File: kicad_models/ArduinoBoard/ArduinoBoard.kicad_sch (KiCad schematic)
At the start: 22 parts, among them J1 5V Output, J10 Conn_01x06_Pin, J2 Buttons, J3 PWM Output, J4 12V Input, J5 Conn_01x04_Pin, J6 Conn_01x04_Pin, J7 Conn_01x06_Pin, J8 Conn_01x06_Pin, J9 Conn_01x04_Pin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

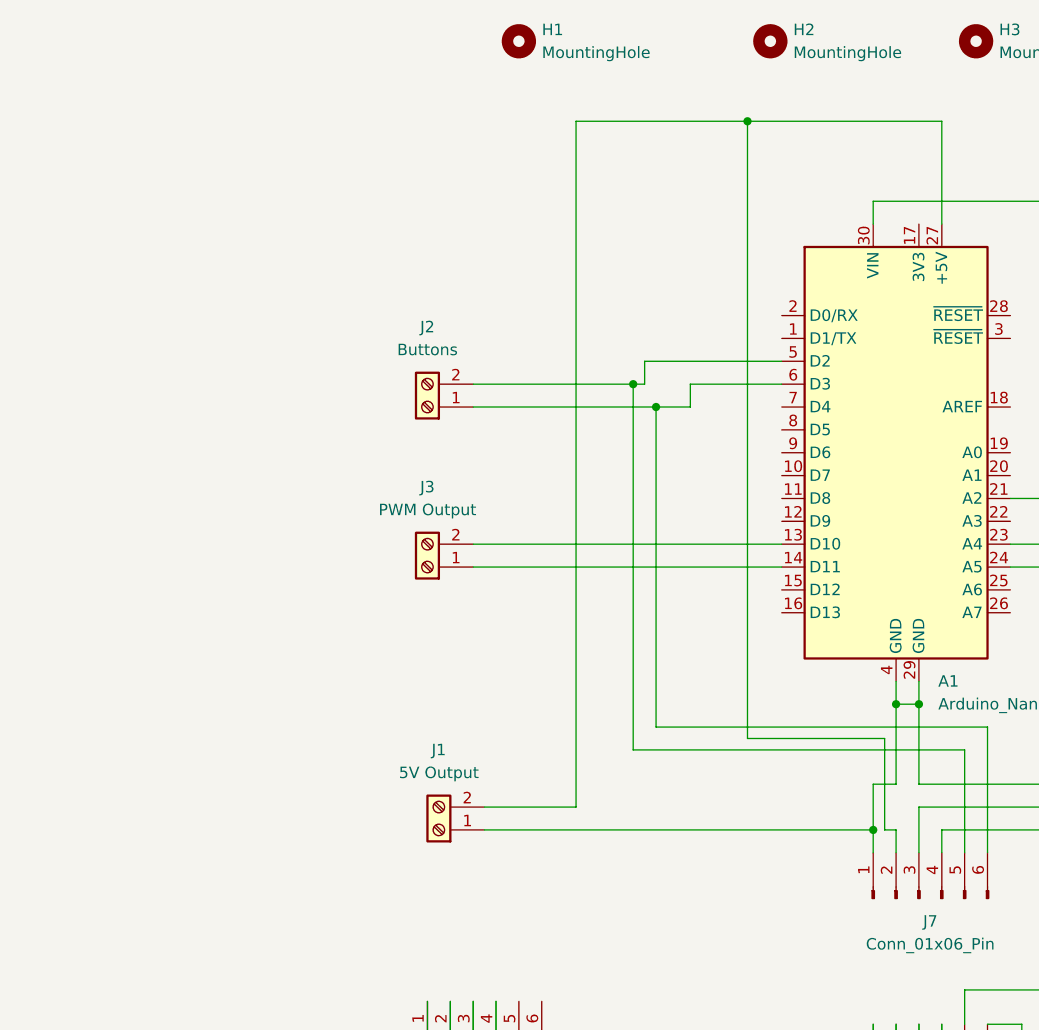
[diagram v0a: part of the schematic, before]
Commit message: Added a 2x4 (8-pin) connector to the main board which allows it to connect to the motor controller with a ribbon cable.
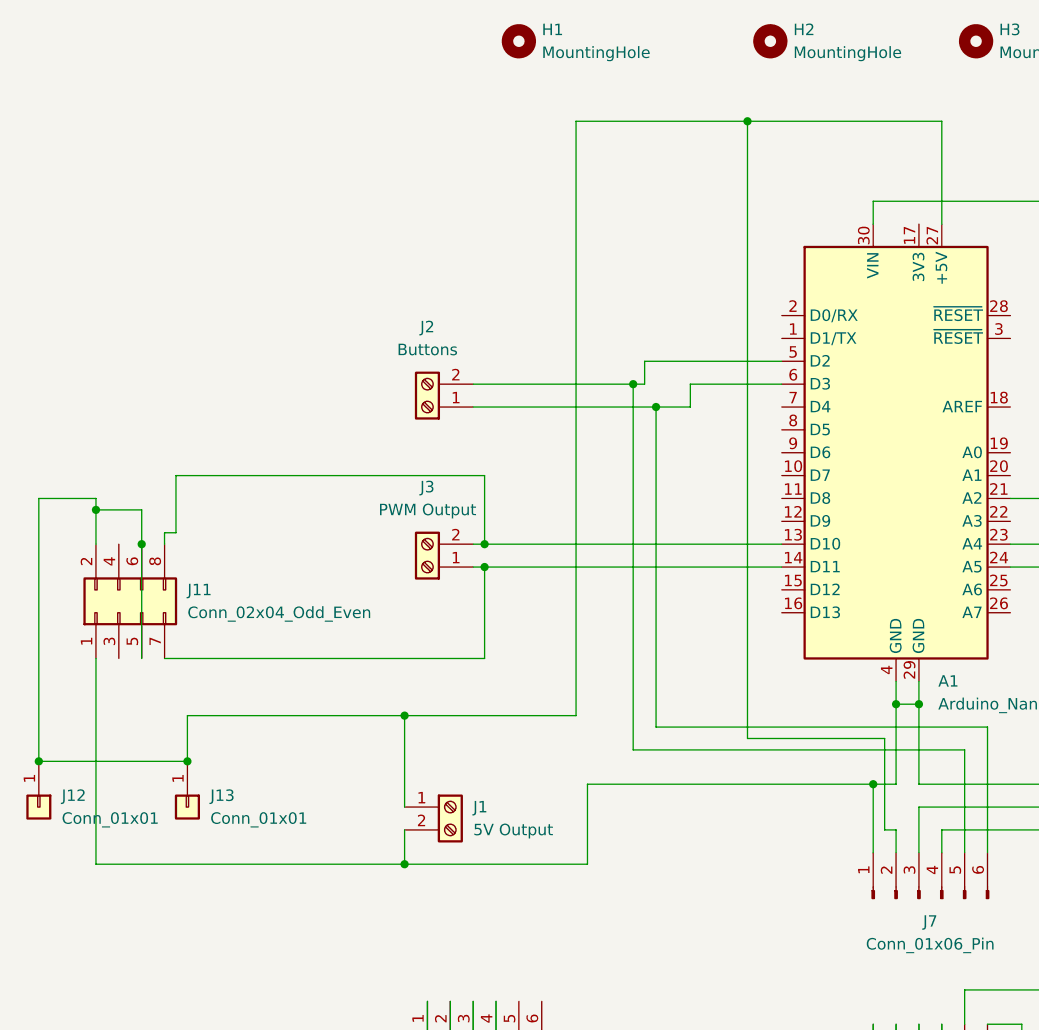
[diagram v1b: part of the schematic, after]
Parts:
- added J11: Conn_02x04_Odd_Even, Connector_PinHeader_2.54mm:PinHeader_2x04_P2.54mm_Vertical, symbol Connector_Generic:Conn_02x04_Odd_Even
- added J12, J13: Conn_01x01, Connector_PinHeader_2.54mm:PinHeader_1x01_P2.54mm_Vertical, symbol Connector_Generic:Conn_01x01
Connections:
- net GND: now also J1.2 (Pin_2), J11.1 (Pin_1); no longer J1.1 (Pin_1)
- net at A1.13 (D10), J3.2 (Pin_2): now also J11.8 (Pin_8)
- net at A1.14 (D11), J3.1 (Pin_1): now also J11.7 (Pin_7)
- net at A1.27 (+5V), J7.2 (Pin_2): now also J1.1 (Pin_1), J11.2 (Pin_2), J11.5 (Pin_5), J11.6 (Pin_6), J12.1 (Pin_1), J13.1 (Pin_1); no longer J1.2 (Pin_2)
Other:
- moved on the sheet: J1

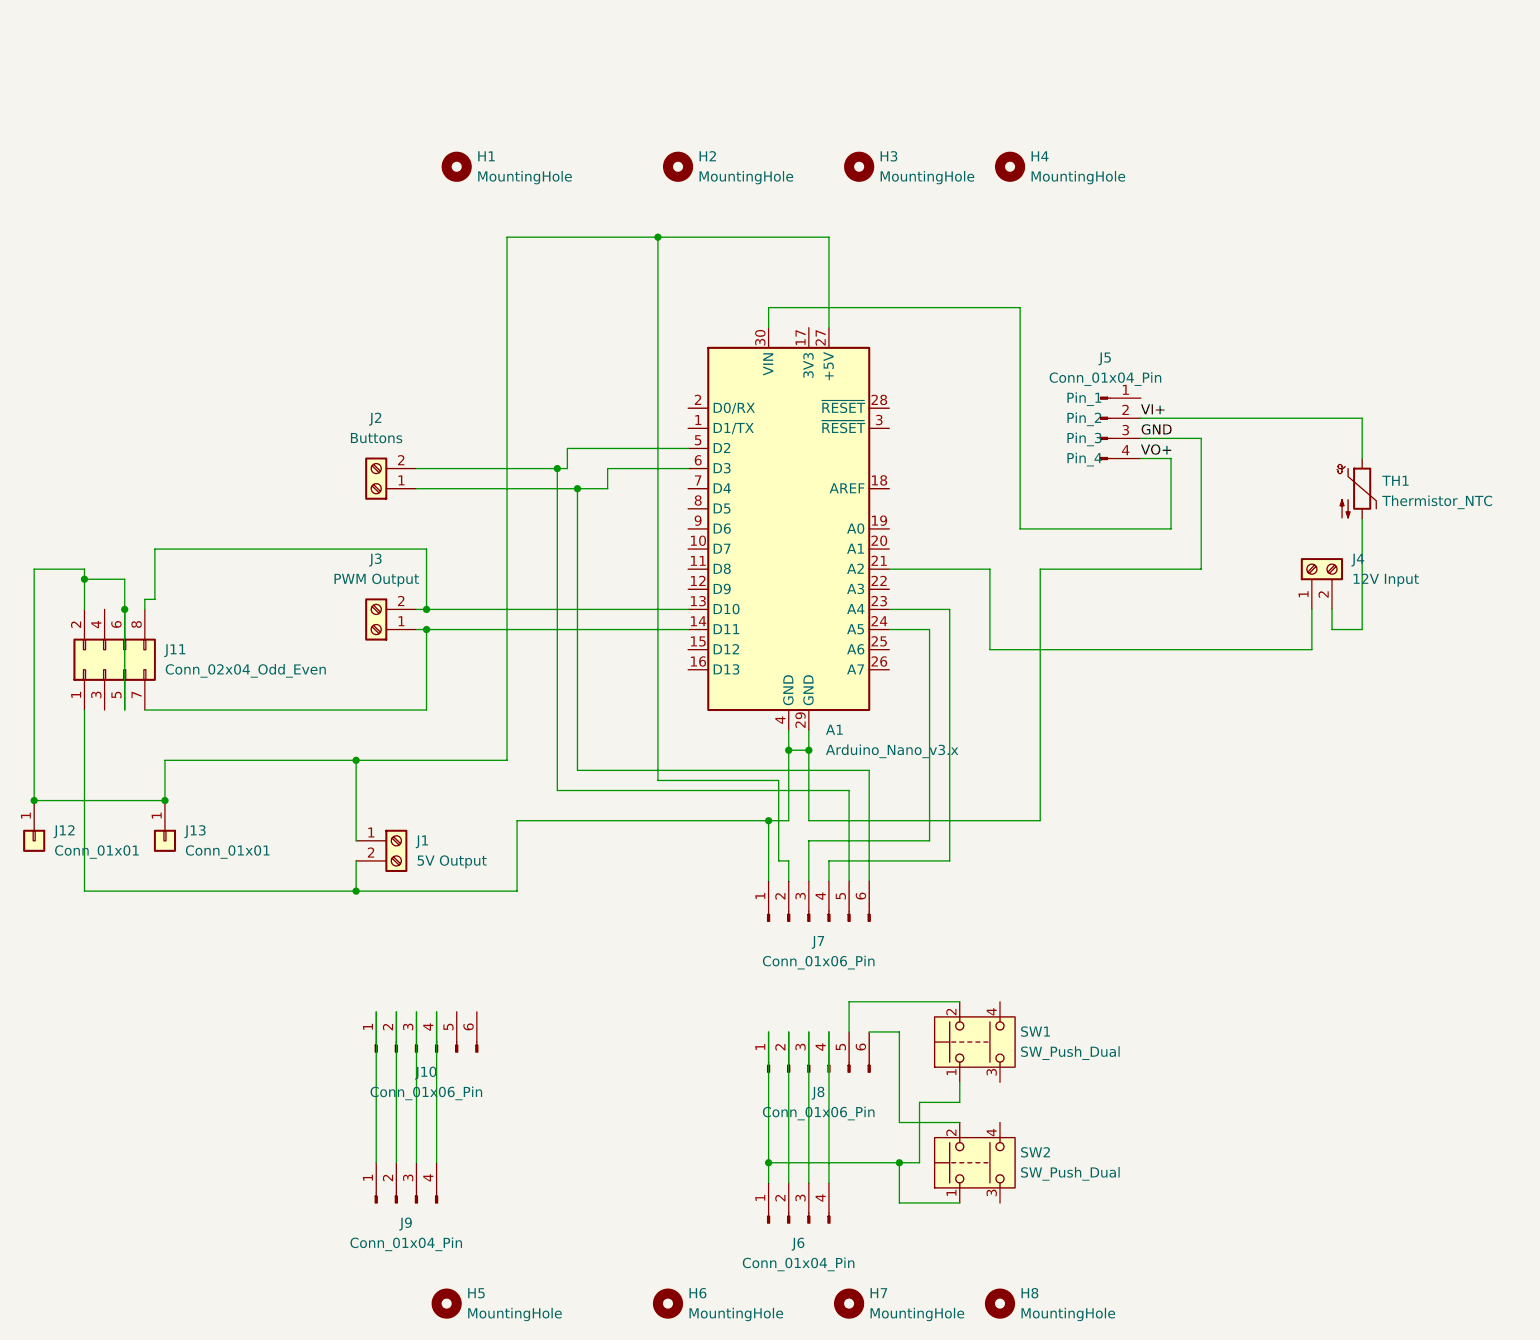
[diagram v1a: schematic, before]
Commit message: Redesigned the PCB - moved the screw terminals for the switch to the other side of the board and changed to analog GPIO (A2 & A3) rather than Digital. Moved the two screw holes that were toward the front of the gauge back about 10mm to give it some space for brass inserts. Updated the Arduino code to use the new GPIO for the switch actuation. Also updated the Solid Edge/STL files to match the new screw holes in the PCB.
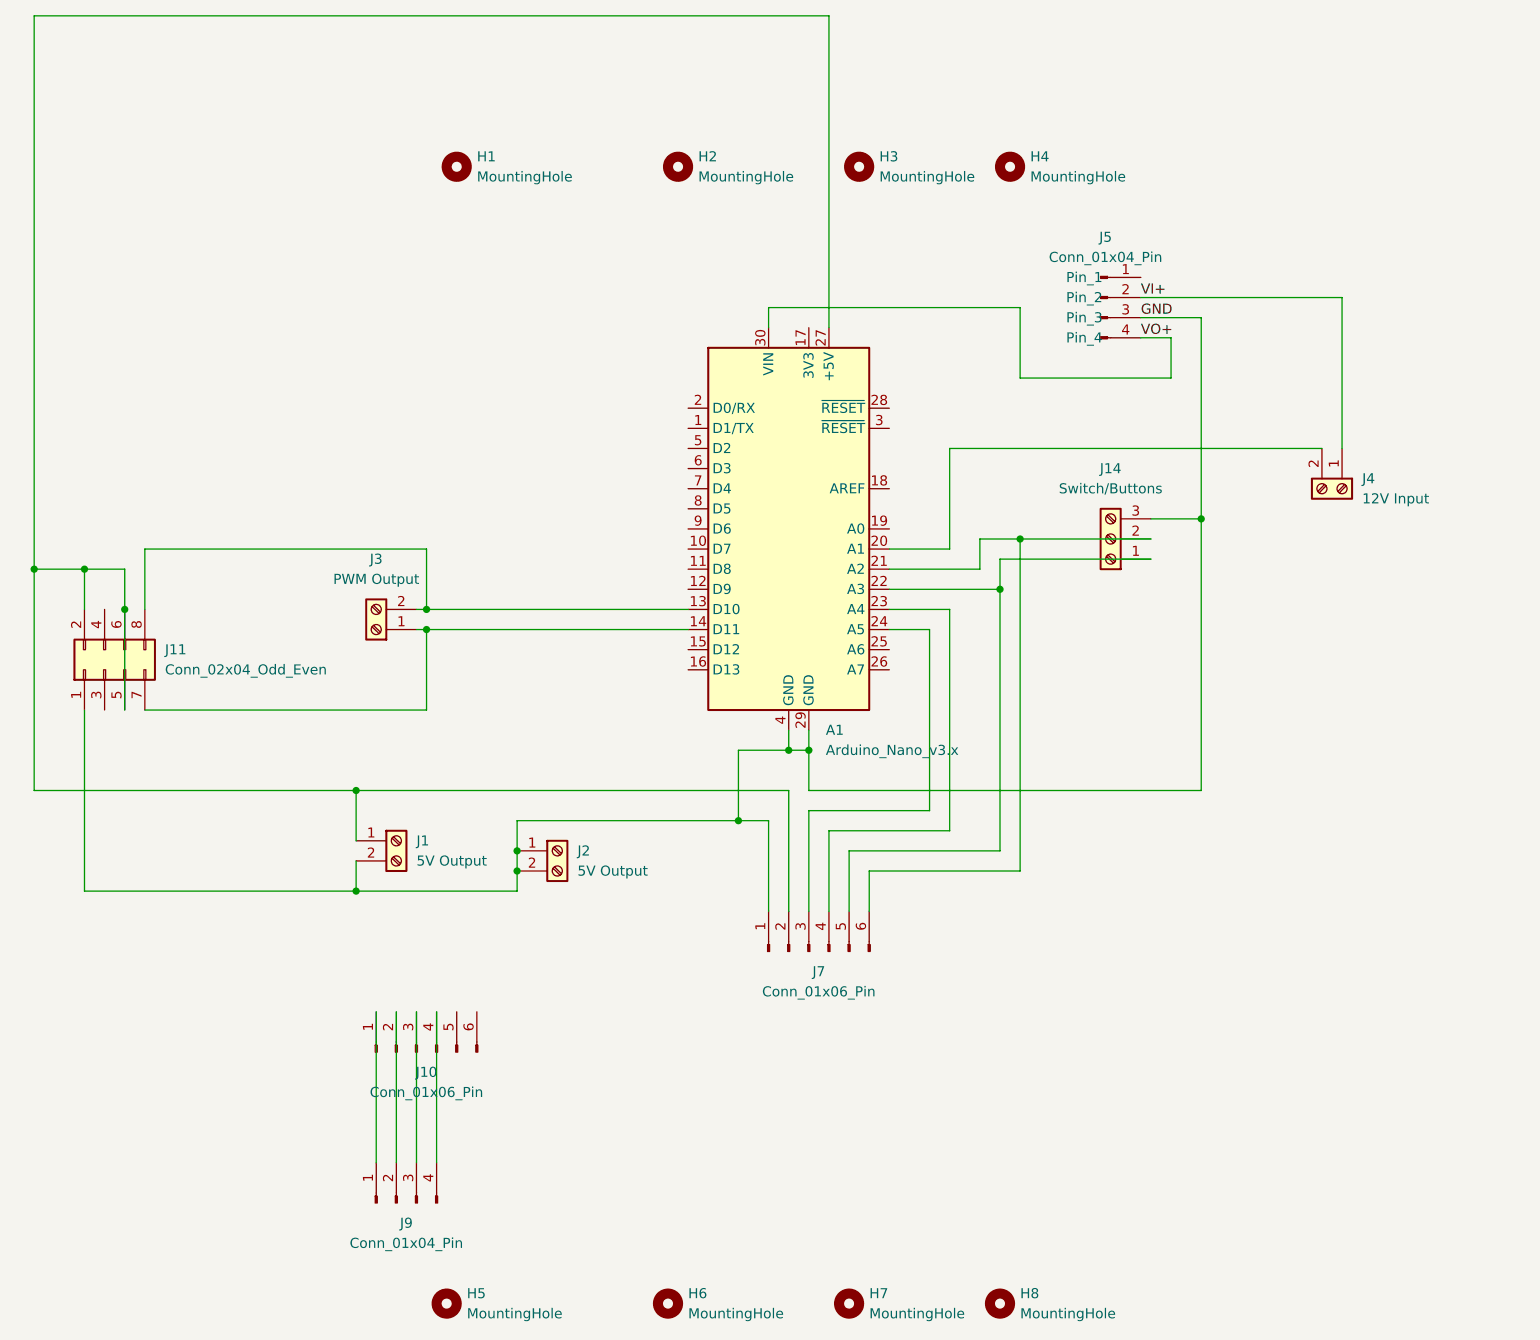
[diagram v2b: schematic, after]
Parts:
- removed J12, J13: Conn_01x01, Connector_PinHeader_2.54mm:PinHeader_1x01_P2.54mm_Vertical, symbol Connector_Generic:Conn_01x01
- removed J6: Conn_01x04_Pin, Connector_PinHeader_2.54mm:PinHeader_1x04_P2.54mm_Vertical, symbol Connector:Conn_01x04_Pin
- removed J8: Conn_01x06_Pin, Connector_PinHeader_2.54mm:PinHeader_1x06_P2.54mm_Vertical, symbol Connector:Conn_01x06_Pin
- removed SW1, SW2: SW_Push_Dual, Button_Switch_THT:SW_PUSH-12mm, symbol Switch:SW_Push_Dual
- removed TH1: Thermistor_NTC, Resistor_THT:R_Axial_DIN0204_L3.6mm_D1.6mm_P5.08mm_Vertical, symbol Device:Thermistor_NTC
- added J14: Switch/Buttons, TerminalBlock:TerminalBlock_bornier-3_P5.08mm, symbol Connector:Screw_Terminal_01x03
- J2: value Buttons -> 5V Output
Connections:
- net GND: now also J2.1 (Pin_1), J2.2 (Pin_2), J14.3 (Pin_3)
- net VI+: now also J4.1 (Pin_1)
- net at J4.2 (Pin_2): now also A1.20 (A1)
- net at A1.21 (A2): now also J7.6 (Pin_6), J14.2 (Pin_2); no longer J4.1 (Pin_1)
- net at A1.22 (A3): now also J7.5 (Pin_5), J14.1 (Pin_1)
- now unconnected: A1.5 (D2), A1.6 (D3)
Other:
- moved on the sheet: J4, J5, J7

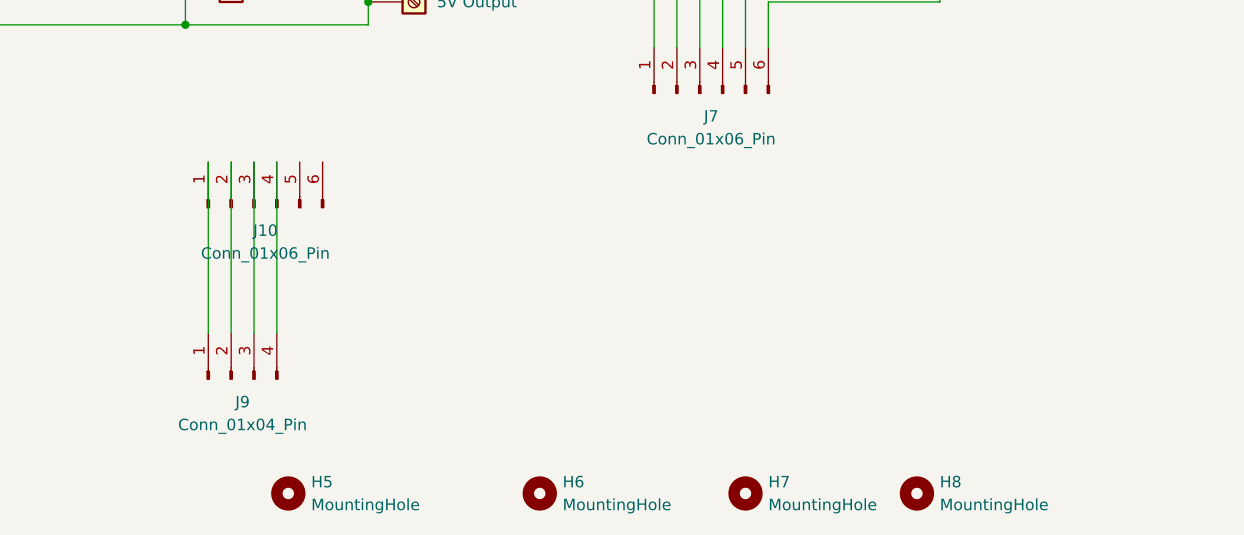
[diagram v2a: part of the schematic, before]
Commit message: Fixed a gerber file issue reported by Jon Parnaby. He noted that a lot of the through holes in the PCBs he ordered from JLCPCB were too small (for Arduino and other components). I grew the holes from .5mm to 1.0mm. I also split the PCB into two separate projects so that it would be easier to send them off to be manufactured.
Also updated the printable PDFs for PCB transfer paper (e.g. reversed, underside, copper-only).
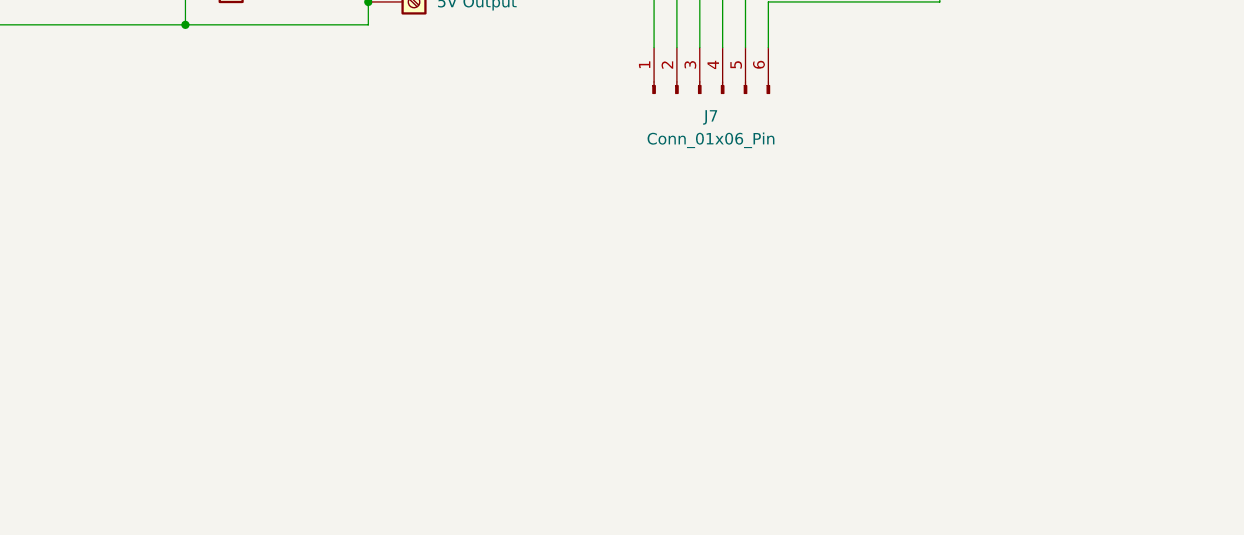
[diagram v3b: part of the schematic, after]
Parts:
- removed H5, H6, H7, H8: MountingHole, MountingHole:MountingHole_2.2mm_M2_DIN965_Pad, symbol Mechanical:MountingHole
- removed J10: Conn_01x06_Pin, Connector_PinHeader_2.54mm:PinHeader_1x06_P2.54mm_Vertical, symbol Connector:Conn_01x06_Pin
- removed J9: Conn_01x04_Pin, Connector_PinHeader_2.54mm:PinHeader_1x04_P2.54mm_Vertical, symbol Connector:Conn_01x04_Pin
